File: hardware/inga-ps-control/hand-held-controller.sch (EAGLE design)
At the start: 6 parts, among them IC1 PCF8574P

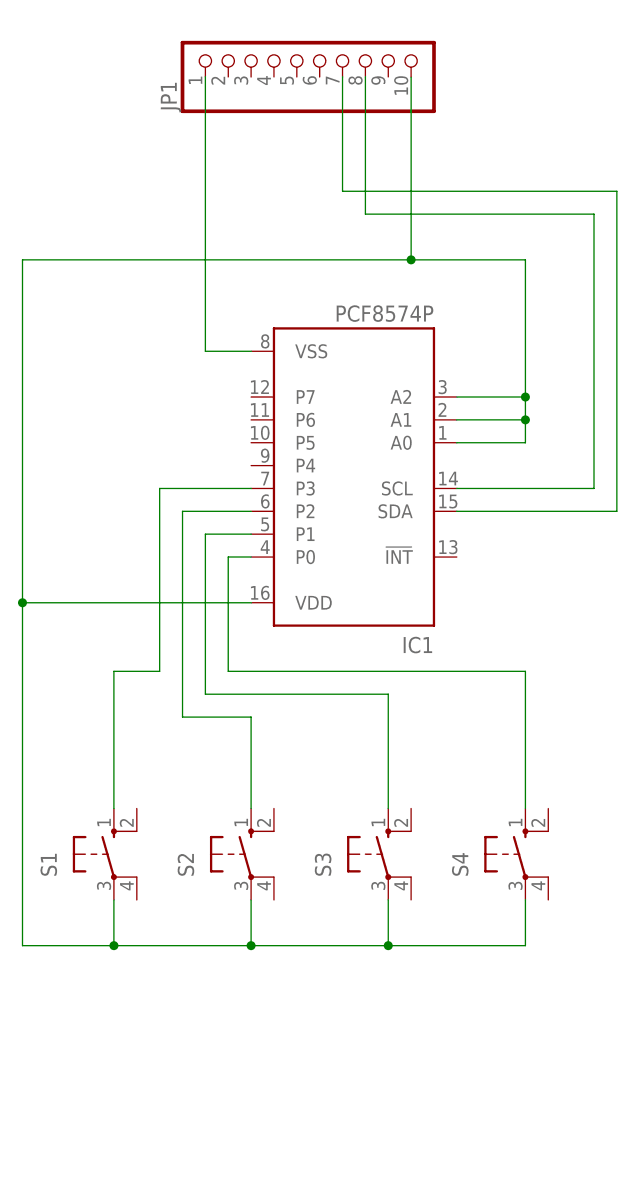
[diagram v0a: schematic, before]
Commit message: some updates for new data protocol
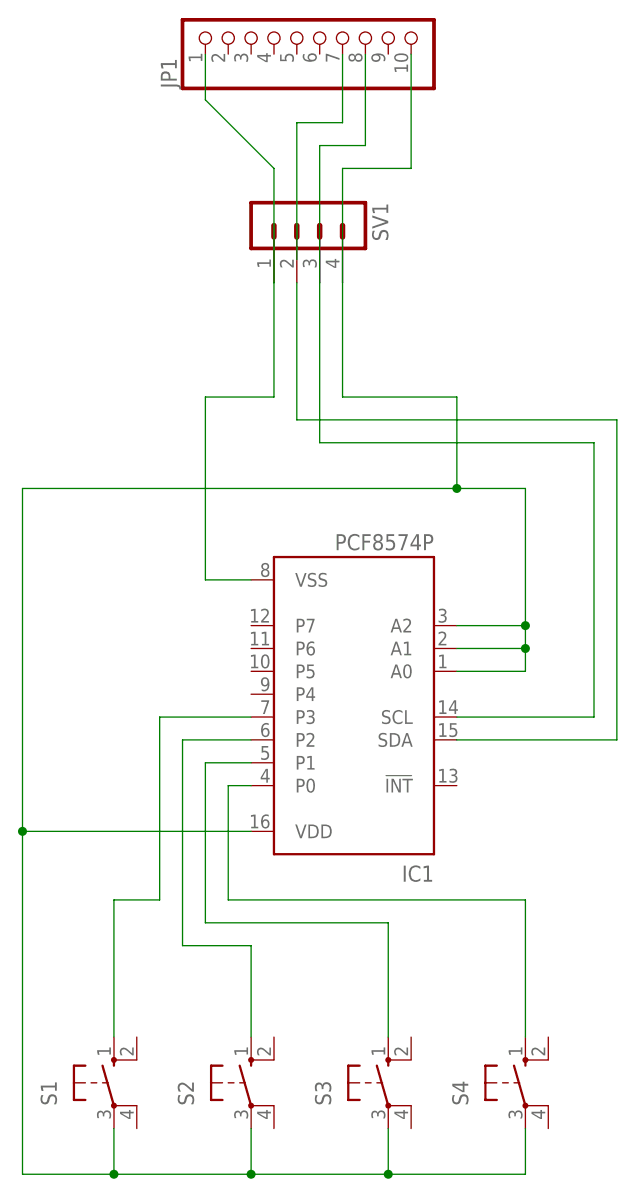
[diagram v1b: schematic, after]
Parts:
- added SV1: (no value), con-lstb:MA04-1
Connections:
- new net N$9: JP1.7
- net N$1: now also SV1.4
- net N$2: now also SV1.1
- net N$3: now also SV1.3
- net N$4: now also SV1.2; no longer JP1.7
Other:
- moved on the sheet: IC1, JP1, S1, S2, S3, S4
